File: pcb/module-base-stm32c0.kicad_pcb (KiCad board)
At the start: 4 copper layers, 50 x 25 mm, 122 parts, among them J1 SWD Header, SW1 SKRPABE010, U1 STM32C031G6Ux, Y1 ECS-480-10-37B2-RWN-TR

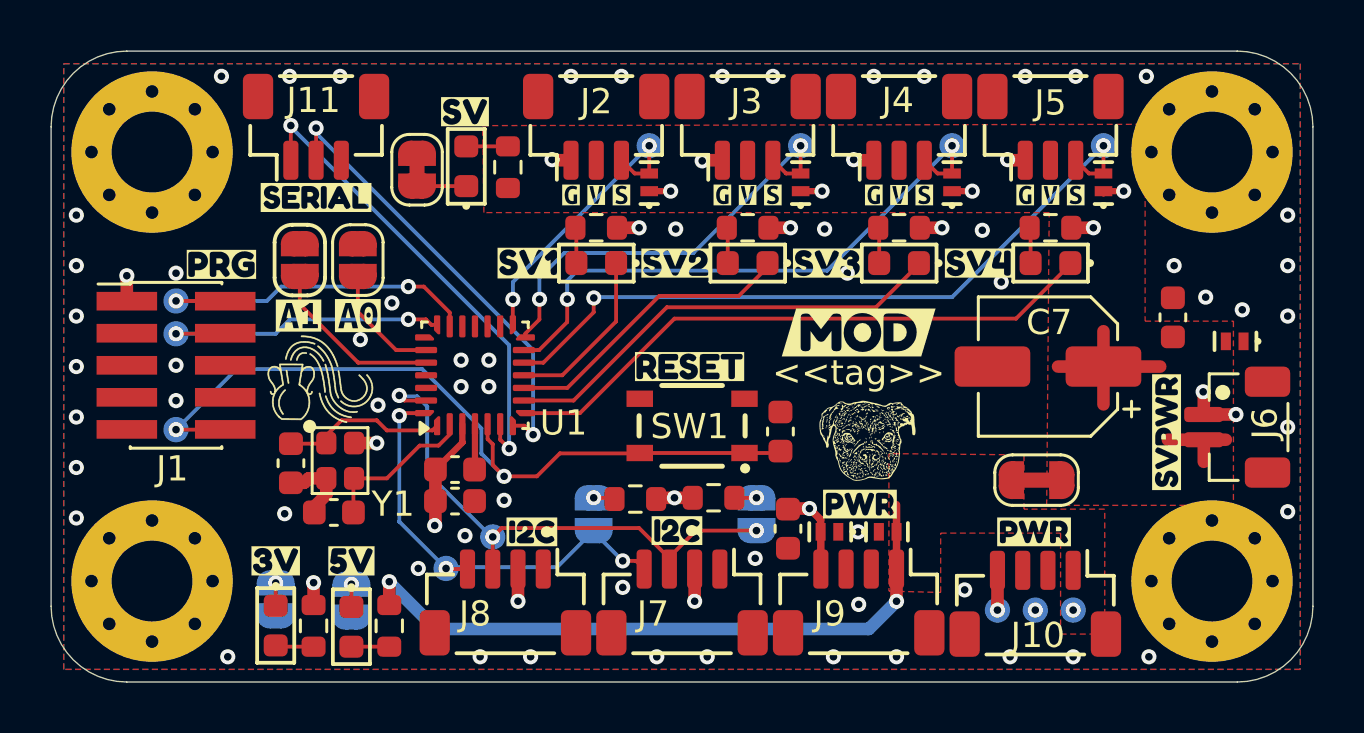
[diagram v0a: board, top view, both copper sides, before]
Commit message: Added guard ring
Optimized layout
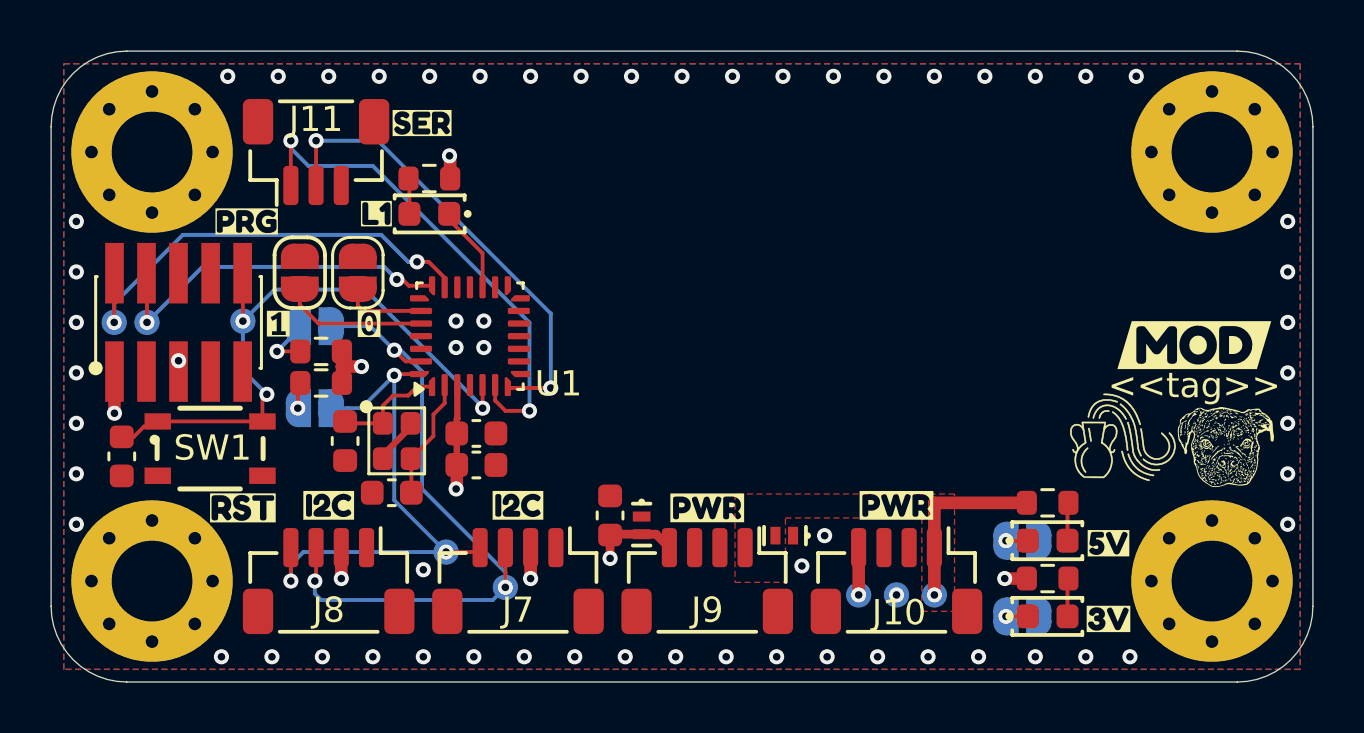
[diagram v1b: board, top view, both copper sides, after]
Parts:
- removed C6: 0.1uF, CRGM Passive:C_0603_1608Metric
- removed C7: 100uF, CRGM Passive:CP_Elec_5x5.4
- removed D14, D2, D3, D4: Blue, CRGM Passive:LED_0603_1608Metric
- removed D5: PESD5V5C1BL, CRGM Passive:DFN1006-2
- removed D6, D7, D8, D9: PESD3V3S1BL, CRGM Passive:DFN1006-2
- removed J2, J3, J4, J5: ~, CRGM Connector:JST_SH_BM03B-SRSS-TB_1x03-1MP_P1.00mm_Vertical
- removed J6: ~, CRGM Connector:JST_SH_BM02B-SRSS-TB_1x02-1MP_P1.00mm_Vertical
- removed JP5: ~, CRGM Connector:SolderJumper-2_P2.0mm_Bridged_RoundedPad1.0x1.5mm
- removed JP8: ~, CRGM Connector:SolderJumper-2_P1.3mm_Bridged_RoundedPad1.0x1.5mm
- removed R4, R5, R6: 1K, CRGM Passive:R_0603_1608Metric
- removed R9: 4.7K, CRGM Passive:R_0603_1608Metric
- removed TP11: SERVO1, CRGM Mechanical:TestPoint_Pad_D1.0mm
- removed TP12: SERVO2, CRGM Mechanical:TestPoint_Pad_D1.0mm
- removed TP13: SERVO3, CRGM Mechanical:TestPoint_Pad_D1.0mm
- removed TP14: SERVO4, CRGM Mechanical:TestPoint_Pad_D1.0mm
- removed kibuzzard-690A7DF7: G***, kibuzzard-690A7DF7
- removed kibuzzard-690A7E03: G***, kibuzzard-690A7E03
- removed kibuzzard-6917608E: G***, kibuzzard-6917608E
- removed kibuzzard-691760A0: G***, kibuzzard-691760A0
- removed kibuzzard-697418BE (x4): G***, kibuzzard-697418BE
- removed kibuzzard-697418CA (x4): G***, kibuzzard-697418CA
- removed kibuzzard-697418D0 (x4): G***, kibuzzard-697418D0
- removed kibuzzard-69B9F676: G***, kibuzzard-69B9F676
- removed kibuzzard-6A29F8F6: G***, kibuzzard-6A29F8F6
- removed kibuzzard-6A2A39A2: G***, kibuzzard-6A2A39A2
- removed kibuzzard-6A2A3A1C: G***, kibuzzard-6A2A3A1C
- removed kibuzzard-6A2A3A22: G***, kibuzzard-6A2A3A22
- removed kibuzzard-6A2A3A2A: G***, kibuzzard-6A2A3A2A
- removed kibuzzard-6A2A3A2F: G***, kibuzzard-6A2A3A2F
- removed kibuzzard-6A2B42C8: G***, kibuzzard-6A2B42C8
- removed kibuzzard-6A2B42D9: G***, kibuzzard-6A2B42D9
- removed kibuzzard-6A2B42F1: G***, kibuzzard-6A2B42F1
- removed kibuzzard-6A2B4302: G***, kibuzzard-6A2B4302
- removed kibuzzard-6A2B4314: G***, kibuzzard-6A2B4314
- removed kibuzzard-6A2B4328: G***, kibuzzard-6A2B4328
- removed kibuzzard-6A2CAB75: G***, kibuzzard-6A2CAB75
- added kibuzzard-6A5157F8: G***, kibuzzard-6A5157F8, F.Cu at (57.6, 103.1)
- added kibuzzard-6A518195: G***, kibuzzard-6A518195, B.Cu at (55.6, 94.1)
- added kibuzzard-6A51A315: G***, kibuzzard-6A51A315, F.Cu at (57.8, 91.8)
- added kibuzzard-6A51A320: G***, kibuzzard-6A51A320, F.Cu at (64.7, 87.8)
- added kibuzzard-6A51A532: G***, kibuzzard-6A51A532, F.Cu at (62.9, 91.4)
- added kibuzzard-6A51AAF7: G***, kibuzzard-6A51AAF7, F.Cu at (62.6, 95.8)
- added kibuzzard-6A51AB05: G***, kibuzzard-6A51AB05, F.Cu at (59.0, 95.8)
- added kibuzzard-6A51AB65: G***, kibuzzard-6A51AB65, F.Cu at (91.9, 107.5)
- added kibuzzard-6A51AB70: G***, kibuzzard-6A51AB70, F.Cu at (91.9, 104.5)
- R7: value 4.7K -> 10K
- R8: value 1K -> 4.7K
- moved kibuzzard-6954A310 32.2 mm to (90.8, 107.5)
- moved LOGO2 31.9 mm to (92.5, 100.2)
- moved D13 30.6 mm to (89.5, 107.4), turned to 0 degrees
- moved JP7 29.6 mm to (88.5, 107.4), turned to 180 degrees
- moved R8 29.1 mm to (89.5, 105.9), turned to 0 degrees
- moved kibuzzard-6954A315 28.9 mm to (90.8, 104.4)
- moved D12 27.8 mm to (89.5, 104.4), turned to 0 degrees
- moved JP6 26.7 mm to (88.5, 104.4), turned to 180 degrees
- moved R7 26.5 mm to (89.5, 102.9), turned to 0 degrees
- moved C5 26.1 mm to (52.8, 101.1), turned to -90 degrees
- moved SW1 19.1 mm to (56.3, 100.8), turned to 0 degrees
- moved JP2 19.0 mm to (60.5, 95.9), turned to 180 degrees
- moved R2 16.6 mm to (60.7, 96.9), turned to 0 degrees
- moved kibuzzard-690D5FD9 15.7 mm to (62.5, 95.8)
- moved LOGO5 14.2 mm to (96.5, 100.7)
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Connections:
- net SWCLK renamed /MCU/SWCLK
- net SWDIO renamed /MCU/SWDIO
- D1 pad 1: /MCU/LED1 -> /MCU/STATUS
- U1 pad 10: /MCU/LED2 -> unconnected-(U1-PA4-Pad10)
- U1 pad 11: /MCU/LED1 -> unconnected-(U1-PA5-Pad11)
- U1 pad 12: SERVO4 -> unconnected-(U1-PA6-Pad12)
- U1 pad 13: SERVO3 -> unconnected-(U1-PA7-Pad13)
- U1 pad 14: SERVO2 -> unconnected-(U1-PB0-Pad14)
- U1 pad 15: SERVO1 -> unconnected-(U1-PB1-Pad15)
- U1 pad 17: unconnected-(U1-PC6-Pad17) -> /MCU/STATUS
- U1 pad 8: /MCU/LED4 -> unconnected-(U1-PA2-Pad8)
- U1 pad 9: /MCU/LED3 -> unconnected-(U1-PA3-Pad9)
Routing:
- net SERVO4: track 29.6 -> 0.00 mm, vias 2 -> 0
- net /MCU/LED4: track 24.0 -> 0.00 mm
- net SERVO3: track 23.9 -> 0.00 mm, vias 2 -> 0
- net +5V: track 26.1 -> 7.31 mm, vias 3 -> 1
- net /MCU/LED3: track 17.9 -> 0.00 mm
- net SERVO2: track 17.8 -> 0.00 mm, vias 2 -> 0
- net GND: track 13.6 -> 1.56 mm, vias 73 -> 61
- net SERVO1: track 12.0 -> 0.00 mm, vias 2 -> 0
- net /MCU/LED2: track 11.6 -> 0.00 mm
- net VSERVO: track 10.1 -> 0.00 mm
- net NRST: track 31.9 -> 24.7 mm, vias 2 -> 3
- net /MCU/LED1: track 6.93 -> 0.00 mm
- net SDA: track 21.5 -> 26.8 mm
- net /MCU/SWDIO: track 13.9 -> 18.0 mm
- net SCL: track 17.7 -> 21.4 mm
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- added copper zone on In2.Cu, net GND
- removed copper zone on In1.Cu, net GND
- removed copper zone on F.Cu, net VSERVO
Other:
- board text added: "/Users/tsasala/Development/pcb//kicad-library"
- board text removed: "#480048FF"
- board text removed: "0"
- board text removed: "0 mm"
- board text removed: "0.01 mm"
- board text removed: "0.0175 mm"
- board text removed: "0.02"
- board text removed: "0.035 mm"
- board text removed: "0.1270 mm / 0.1524 mm"
- board text removed: "0.2 mm"
- board text removed: "0.2500 mm"
- board text removed: "1"
- board text removed: "1.075 mm"
- board text removed: "1.6000 mm"
- board text removed: "3.3"
- board text removed: "4"
- board text removed: "4.5"
- board text removed: "50.0000 mm x 25.0000 mm"
- board text removed: "B.Cu"
- board text removed: "B.Mask"
- board text removed: "B.Paste"
- board text removed: "B.Silkscreen"
- board text removed: "BOARD CHARACTERISTICS"
- board text removed: "Board Thickness:"
- board text removed: "Board overall dimensions:"
- board text removed: "Bottom Silk Screen"
- board text removed: "Bottom Solder Mask"
- board text removed: "Bottom Solder Paste"
- board text removed: "Castellated pads:"
- board text removed: "Color"
- board text removed: "Copper Finish:"
- board text removed: "Copper Layer Count:"
- board text removed: "Dielectric 1"
- board text removed: "Dielectric 2"
- board text removed: "Dielectric 3"
- board text removed: "Edge card connectors:"
- board text removed: "Epsilon R"
- board text removed: "F.Cu"
- board text removed: "F.Mask"
- board text removed: "F.Paste"
- board text removed: "F.Silkscreen"
- board text removed: "FR4"
- board text removed: "HAL SnPb"
- board text removed: "Impedance Control:"
- board text removed: "In1.Cu"
- board text removed: "In2.Cu"
- board text removed: "Layer Name"
- board text removed: "Loss Tangent"
- board text removed: "Material"
- board text removed: "Min hole diameter:"
- board text removed: "Min track/spacing:"
- board text removed: "No"
- board text removed: "Not specified"
- board text removed: "Plated Board Edge:"
- board text removed: "Thickness (mm)"
- board text removed: "Top Silk Screen"
- board text removed: "Top Solder Mask"
- board text removed: "Top Solder Paste"
- board text removed: "Type"
- board text removed: "White"
- board text removed: "copper"
- board text removed: "core"
- board text removed: "prepreg"
